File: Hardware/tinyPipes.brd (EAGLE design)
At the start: 59 x 59 mm, 94 parts, among them Q1 CJ2302, Q5 S9013, Q6 S9013, Q7 S9013, U1 TD1410, U2 ICS_V54_SIM900, U3 ATMEGA168, U4 MAX4372, U5 SI4435POWER

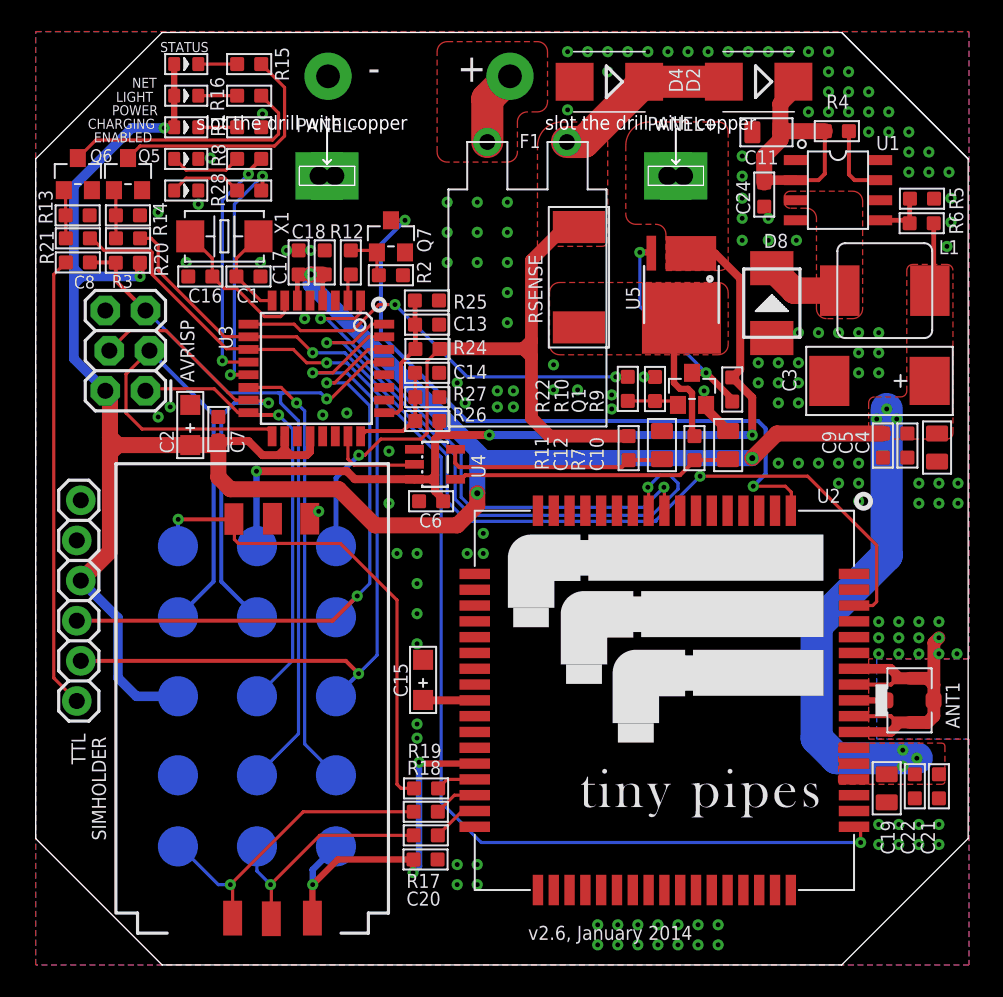
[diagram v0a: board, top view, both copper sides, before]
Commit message: added gerber files for the PCB and a signal strength utility in the utilities folder
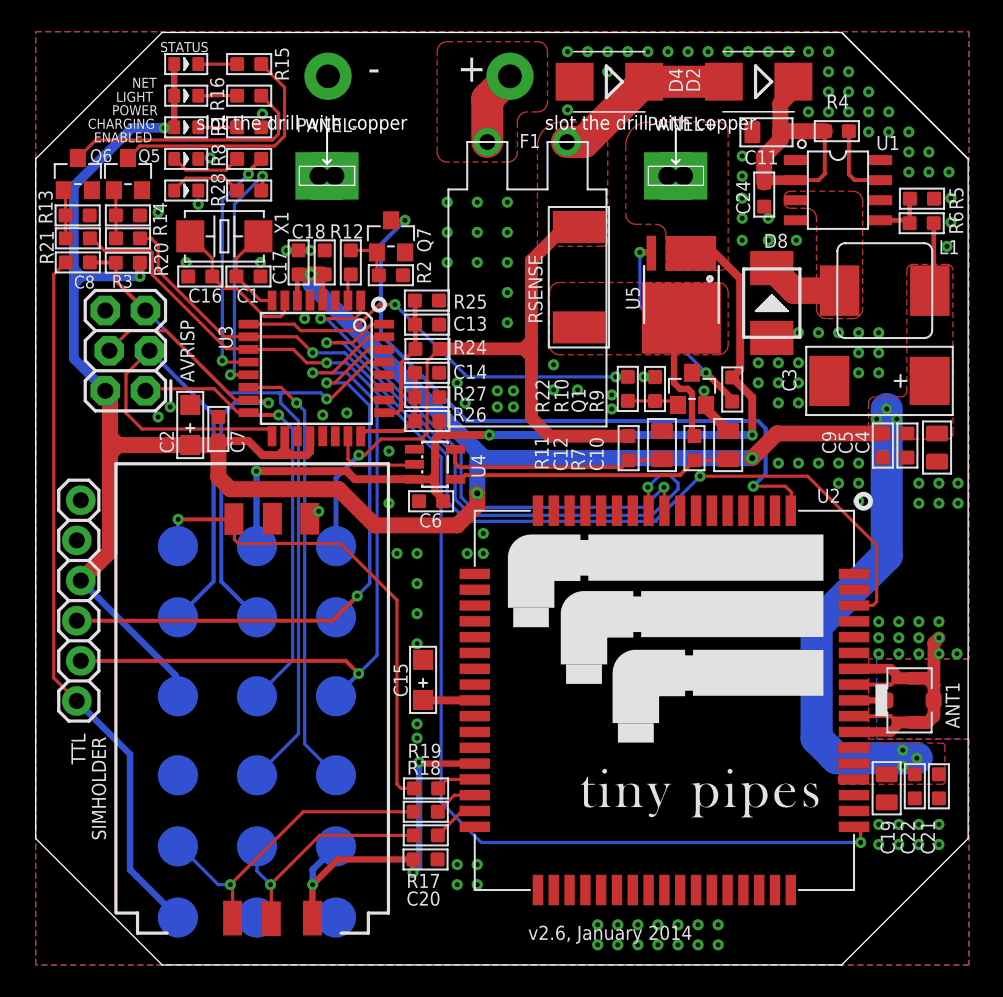
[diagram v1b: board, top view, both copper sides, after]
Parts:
- added DTR, GND1, GND2: PTR1B2,54, testpad:B2,54
- AVRISP: value AVR_SPI_PRG_62X3_LOCK -> DNP
- R24, R26: value 39k -> 39k,1%
- R25, R27, R5: value 10k -> 10k,1%
- R6: value 24k -> 24k,1%
- RSENSE: value 0.003 -> 0.003R,1%
- TTL: value (none) -> DNP
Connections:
- net DTR: now also DTR.TP
- net GND: now also GND1.TP, GND2.TP
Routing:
- net DTR: track 28.7 -> 45.0 mm
- net VCC: track 179.2 -> 177.7 mm
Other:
- board text added: "GND"
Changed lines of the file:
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@@
 <wire x1="50.8" y1="16.383" x2="50.8" y2="17.145" width="0.2032" layer="41"/>
 <rectangle x1="52.705" y1="40.767" x2="54.61" y2="44.577" layer="41"/>
-<text x="10.795" y="3.81" size="0.889" layer="22" ratio="11" rot="MR0">SIM_CLK</text>
-<text x="16.764" y="3.81" size="0.889" layer="22" ratio="11" rot="MR0">SIM_RST</text>
-<text x="22.86" y="3.81" size="0.889" layer="22" ratio="11" rot="MR0">SIM_VDD</text>
+<text x="10.414" y="4.826" size="0.889" layer="22" ratio="11" rot="MR0">SIM_CLK</text>
+<text x="16.129" y="4.826" size="0.889" layer="22" ratio="11" rot="MR0">SIM_RST</text>
+<text x="21.717" y="4.826" size="0.889" layer="22" ratio="11" rot="MR0">SIM_VDD</text>
 <text x="11.176" y="28.194" size="0.889" layer="22" ratio="11" rot="MR0">SIM_IO</text>
+<text x="15.113" y="0.381" size="0.889" layer="22" ratio="11" rot="MR0">GND</text>
+<text x="20.193" y="0.381" size="0.889" layer="22" ratio="11" rot="MR0">GND</text>
 </plain>
 <attributes>
@@
 <attribute name="VALUE" x="51.71" y="52.9455" size="0.4064" layer="27" ratio="10" rot="R180"/>
 </element>
-<element name="R5" library="Discrete" package="R0603" value="10k" x="56.08" y="48.483" smashed="yes">
+<element name="R5" library="Discrete" package="R0603" value="10k,1%" x="56.08" y="48.483" smashed="yes">
 <attribute name="NAME" x="58.7" y="47.78" size="0.889" layer="25" ratio="11" rot="R90"/>
 <attribute name="VALUE" x="54.429" y="47.0225" size="0.635" layer="27" ratio="10"/>
 </element>
-<element name="R6" library="Discrete" package="R0603" value="24k" x="56.06" y="46.93" smashed="yes">
+<element name="R6" library="Discrete" package="R0603" value="24k,1%" x="56.06" y="46.93" smashed="yes">
 <attribute name="NAME" x="58.688" y="46.222" size="0.889" layer="25" ratio="11" rot="R90"/>
 <attribute name="VALUE" x="54.409" y="45.4695" size="0.635" layer="27" ratio="10"/>
@@
 <attribute name="NAME" x="12.468" y="38.964" size="0.889" layer="25" ratio="11" rot="R90"/>
 </element>
-<element name="AVRISP" library="SparkFun" package="2X3_LOCK" value="AVR_SPI_PRG_62X3_LOCK" x="6.946" y="36.328" smashed="yes" rot="R90">
+<element name="AVRISP" library="SparkFun" package="2X3_LOCK" value="DNP" x="6.946" y="36.328" smashed="yes" rot="R90">
 <attribute name="NAME" x="10.039" y="36.869" size="0.889" layer="25" ratio="11" rot="R90"/>
 </element>
@@
 <attribute name="VALUE" x="37.772" y="37.0765" size="0.6096" layer="27" rot="R270"/>
 </element>
-<element name="RSENSE" library="Discrete" package="R2512" value="0.003" x="34.373" y="43.513" smashed="yes" rot="R270">
+<element name="RSENSE" library="Discrete" package="R2512" value="0.003R,1%" x="34.373" y="43.513" smashed="yes" rot="R270">
 <attribute name="NAME" x="32.067" y="40.58" size="0.889" layer="25" ratio="11" rot="R90"/>
 <attribute name="VALUE" x="32.268" y="46.734" size="0.6096" layer="27" rot="R270"/>
 </element>
-<element name="R24" library="Discrete" package="R0603" value="39k" x="24.788" y="38.973" smashed="yes">
+<element name="R24" library="Discrete" package="R0603" value="39k,1%" x="24.788" y="38.973" smashed="yes">
 <attribute name="NAME" x="26.4105" y="38.638" size="0.889" layer="25" ratio="11"/>
 <attribute name="VALUE" x="24.407" y="37.83" size="0.6096" layer="27"/>
 </element>
-<element name="R25" library="Discrete" package="R0603" value="10k" x="24.7545" y="42.0395" smashed="yes" rot="R180">
+<element name="R25" library="Discrete" package="R0603" value="10k,1%" x="24.7545" y="42.0395" smashed="yes" rot="R180">
 <attribute name="NAME" x="26.4265" y="41.5265" size="0.889" layer="25" ratio="11"/>
 <attribute name="VALUE" x="25.3895" y="43.4365" size="0.6096" layer="27" rot="R180"/>
 </element>
-<element name="R26" library="Discrete" package="R0603" value="39k" x="24.779" y="34.4145" smashed="yes">
+<element name="R26" library="Discrete" package="R0603" value="39k,1%" x="24.779" y="34.4145" smashed="yes">
 <attribute name="NAME" x="26.384" y="34.3875" size="0.889" layer="25" ratio="11"/>
 <attribute name="VALUE" x="25.414" y="33.0175" size="0.6096" layer="27"/>
 </element>
-<element name="R27" library="Discrete" package="R0603" value="10k" x="24.779" y="35.9235" smashed="yes" rot="R180">
+<element name="R27" library="Discrete" package="R0603" value="10k,1%" x="24.779" y="35.9235" smashed="yes" rot="R180">
 <attribute name="NAME" x="26.402" y="35.7045" size="0.889" layer="25" ratio="11"/>
 <attribute name="VALUE" x="26.462" y="35.2885" size="0.6096" layer="27" rot="R180"/>
@@
 <attribute name="VALUE" x="44.967" y="52.4305" size="0.4064" layer="27" ratio="10"/>
 </element>
-<element name="TTL" library="SparkFun-Connectors" package="1X06_LOCK" value="" x="2.6" y="16.7" smashed="yes" rot="R90">
+<element name="TTL" library="SparkFun-Connectors" package="1X06_LOCK" value="DNP" x="2.6" y="16.7" smashed="yes" rot="R90">
 <attribute name="NAME" x="3.149" y="12.692" size="0.889" layer="25" font="vector" ratio="11" rot="R90"/>
 <attribute name="VALUE" x="5.902" y="15.43" size="1.27" layer="27" font="vector" rot="R90"/>
@@
 <attribute name="VALUE" x="14.986" y="49.149" size="1.27" layer="27" ratio="10" rot="R180"/>
 <attribute name="NAME" x="12.7" y="46.228" size="0.3048" layer="33" ratio="10" rot="R180"/>
+</element>
+<element name="DTR" library="testpad" package="B2,54" value="PTR1B2,54" x="9" y="3" smashed="yes" rot="MR0">
+<attribute name="TP_SIGNAL_NAME" value="" x="10.27" y="-0.175" size="1" layer="38" rot="MR0"/>
+<attribute name="NAME" x="10.143" y="0.333" size="0.889" layer="26" ratio="11" rot="MR0"/>
+<attribute name="VALUE" x="10.27" y="1.603" size="0.0254" layer="28" rot="MR0"/>
+</element>
+<element name="GND1" library="testpad" package="B2,54" value="PTR1B2,54" x="14" y="3" smashed="yes" rot="MR0">
+<attribute name="TP_SIGNAL_NAME" value="" x="15.27" y="-0.175" size="1" layer="38" rot="MR0"/>
+<attribute name="VALUE" x="15.27" y="1.603" size="0.0254" layer="28" rot="MR0"/>
+</element>
+<element name="GND2" library="testpad" package="B2,54" value="PTR1B2,54" x="19" y="3" smashed="yes" rot="MR0">
+<attribute name="TP_SIGNAL_NAME" value="" x="20.27" y="-0.175" size="1" layer="38" rot="MR0"/>
+<attribute name="VALUE" x="20.27" y="1.603" size="0.0254" layer="28" rot="MR0"/>
 </element>
 </elements>
@@
 <via x="29.21" y="35.306" extent="1-16" drill="0.3048" diameter="0.635"/>
 <contactref element="PANEL-" pad="P$2"/>
+<contactref element="GND1" pad="TP"/>
+<contactref element="GND2" pad="TP"/>
 </signal>
 <signal name="SIM_DATA">
@@
 <wire x1="27.94" y1="32.512" x2="17.399" y2="43.053" width="1.016" layer="16"/>
 <wire x1="17.399" y1="43.053" x2="17.399" y2="43.688" width="1.016" layer="16"/>
-<wire x1="9" y1="17" x2="6.368" y2="17" width="0.6096" layer="16"/>
-<wire x1="6.368" y1="17" x2="5.207" y2="18.161" width="0.6096" layer="16"/>
-<wire x1="5.207" y1="18.161" x2="5.207" y2="21.967" width="0.6096" layer="16"/>
-<wire x1="5.207" y1="21.967" x2="2.854" y2="24.32" width="0.6096" layer="16"/>
 <wire x1="11.557" y1="33.147" x2="11.557" y2="32.893" width="1.016" layer="1"/>
 <wire x1="11.557" y1="32.893" x2="9.652" y2="32.893" width="1.016" layer="1"/>
@@
 <wire x1="46.8975" y1="33.626" x2="45.339" y2="32.0675" width="1.016" layer="1"/>
 <via x="45.339" y="32.0675" extent="1-16" drill="0.381" diameter="0.8128"/>
-<wire x1="45.339" y1="32.0675" x2="29.23386875" y2="32.0675" width="1.016" layer="16"/>
+<wire x1="45.339" y1="32.0675" x2="28.5115" y2="32.0675" width="1.016" layer="16"/>
 <wire x1="28.5115" y1="32.0675" x2="28.3845" y2="32.0675" width="1.016" layer="16"/>
 <wire x1="28.3845" y1="32.0675" x2="27.94" y2="32.512" width="1.016" layer="16"/>
@@
 <wire x1="26.67" y1="27.813" x2="27.94" y2="29.083" width="1.016" layer="1"/>
 <wire x1="27.94" y1="29.083" x2="27.94" y2="29.845" width="1.016" layer="1"/>
-<wire x1="29.23386875" y1="32.0675" x2="28.5115" y2="32.0675" width="1.016" layer="16"/>
 <wire x1="28.5115" y1="32.0675" x2="27.94" y2="31.496" width="1.016" layer="16"/>
+<wire x1="2.854" y1="24.32" x2="2.858" y2="24.32" width="0.4064" layer="16"/>
+<wire x1="8.845925" y1="17.154075" x2="9" y2="17" width="0.4064" layer="16"/>
+<wire x1="8.845925" y1="17.154075" x2="8.845925" y2="18.332075" width="0.4064" layer="16"/>
+<wire x1="8.845925" y1="18.332075" x2="2.858" y2="24.32" width="0.4064" layer="16"/>
 </signal>
 <signal name="GSM_POWER">
@@
 <wire x1="1.905" y1="44.45" x2="1.143" y2="43.688" width="0.2032" layer="1"/>
 <wire x1="1.143" y1="43.688" x2="1.143" y2="18.157" width="0.2032" layer="1"/>
+<contactref element="DTR" pad="TP"/>
+<wire x1="2.6" y1="16.7" x2="2.604" y2="16.7" width="0.4064" layer="16"/>
+<wire x1="2.604" y1="16.7" x2="5.969" y2="13.335" width="0.4064" layer="16"/>
+<wire x1="5.969" y1="13.335" x2="5.969" y2="6.031" width="0.4064" layer="16"/>
+<wire x1="5.969" y1="6.031" x2="6.412" y2="5.588" width="0.4064" layer="16"/>
+<wire x1="6.412" y1="5.588" x2="9" y2="3" width="0.4064" layer="16"/>
 </signal>
 <signal name="N$2">

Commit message: cleaned up master
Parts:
- removed C10, C12: 100nF, Discrete:C0805
- removed R11, R7: 10k, Discrete:R0603
- added C23: 100nF, Discrete:C0805
- added R23: 10k, Discrete:R0603
- moved U4 0.34 mm to (25.6, 31.8)
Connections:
- new net ALT: U3.26
- new net ALT2: U3.27
- new net ALT3: U3.28
- new net ALT5: U3.22
- new net N$17: R23.1, U4.2
- new net `: U3.19
- net BATTERY: no longer R11.1
- net GND: now also C23.1; no longer C10.2, C12.2
- net PANEL_CURRENT: now also C23.2, R23.2; no longer U4.2
- net PANEL_SWITCH: no longer R7.1
- net RSENSE+: no longer C10.1, R7.2
- net RSENSE-: no longer C12.1, R11.2
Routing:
- net PANEL_SWITCH: track 8.60 -> 0.00 mm
- net RSENSE+: track 17.8 -> 25.3 mm
- net BATTERY: track 55.7 -> 50.7 mm
- net RSENSE-: track 14.7 -> 19.1 mm
- net GND: track 24.4 -> 22.4 mm
- net N$17: track 0.00 -> 1.48 mm
- net VCC: track 177.7 -> 178.7 mm
- net PANEL_CURRENT: track 5.83 -> 6.59 mm, vias 0 -> 2
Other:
- board text added: "v2.7 february 2014"
- board text removed: "v2.6, January 2014"
